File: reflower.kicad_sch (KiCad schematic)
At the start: 46 parts, among them J1 Jack-DC, SW1 RotaryEncoder_Switch, U1 AT32UC3B0256, U2 NCP1117-3.3, U3 MAX6675ISA+

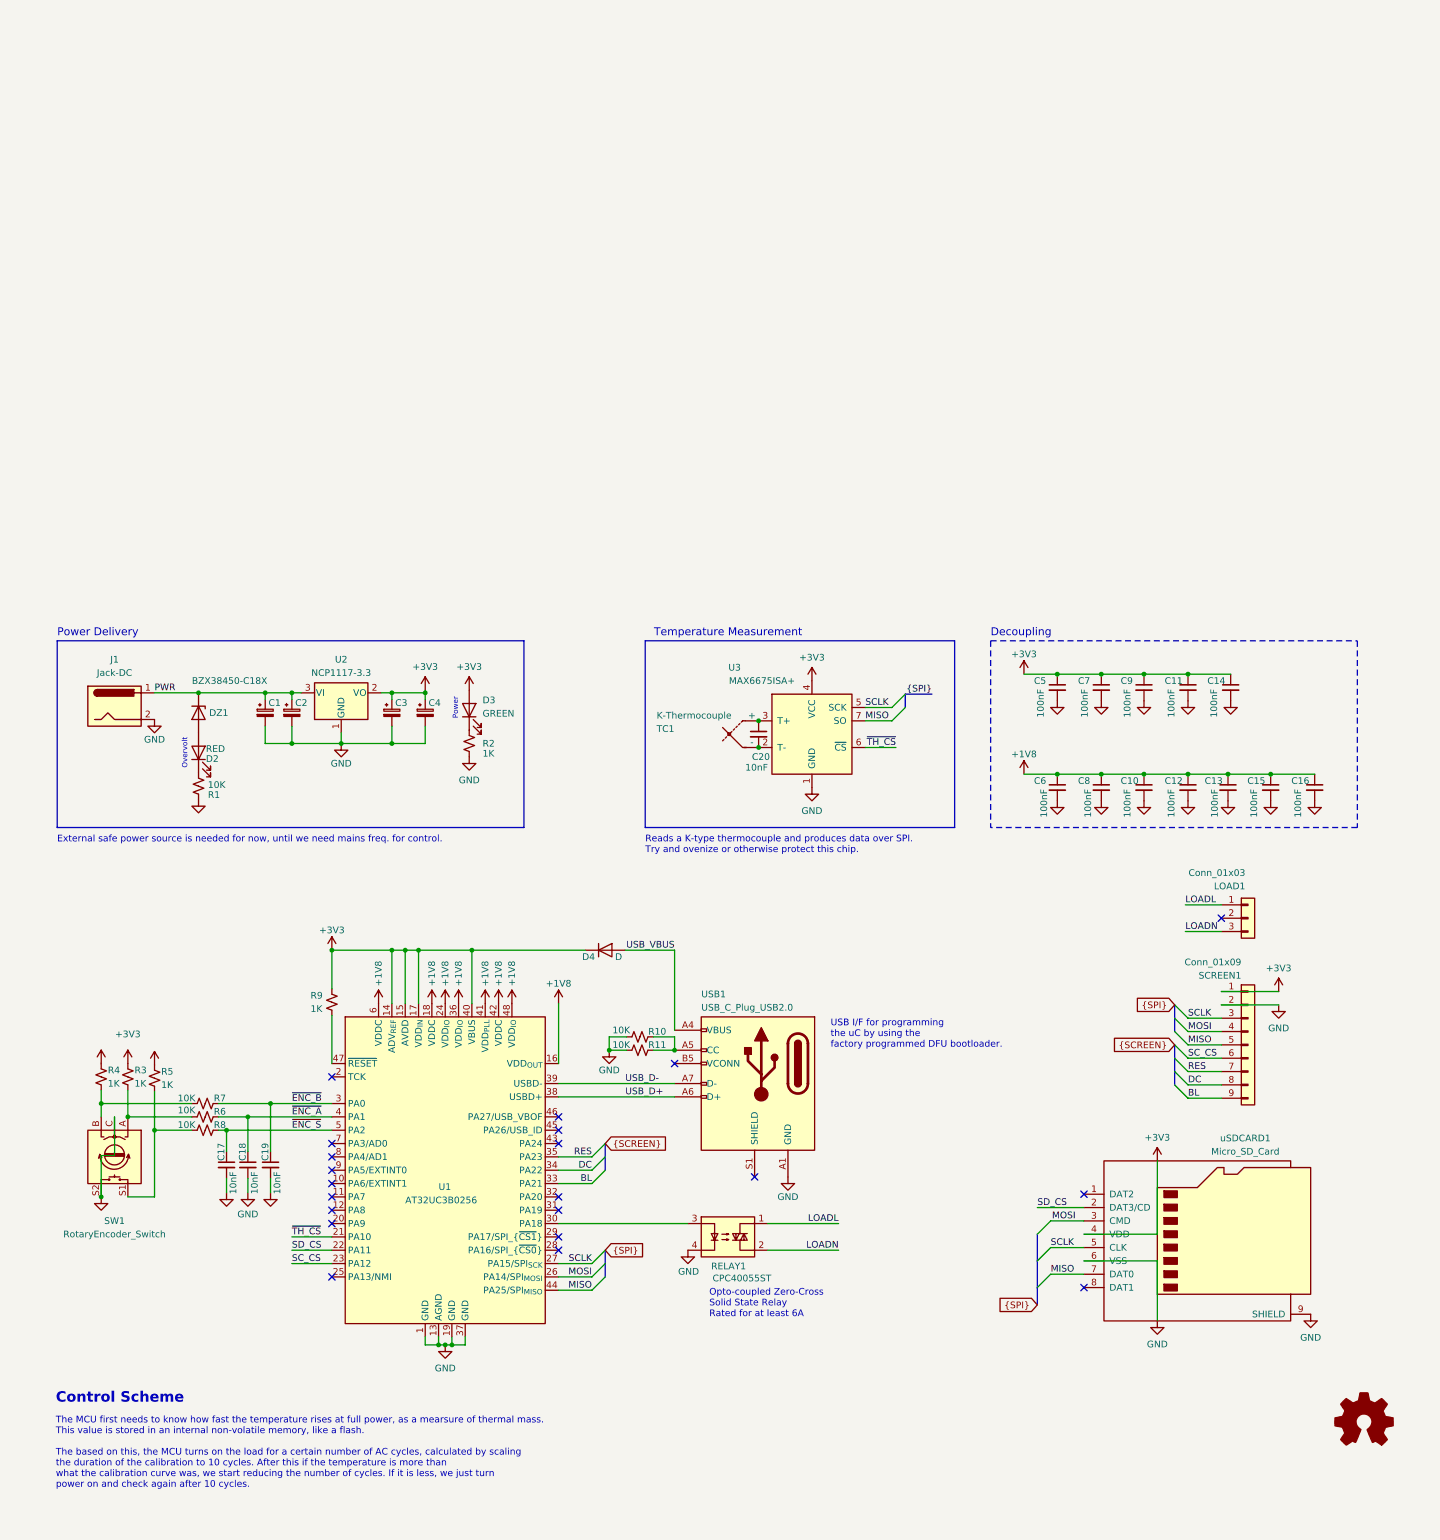
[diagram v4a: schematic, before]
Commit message: Revise to use STM32
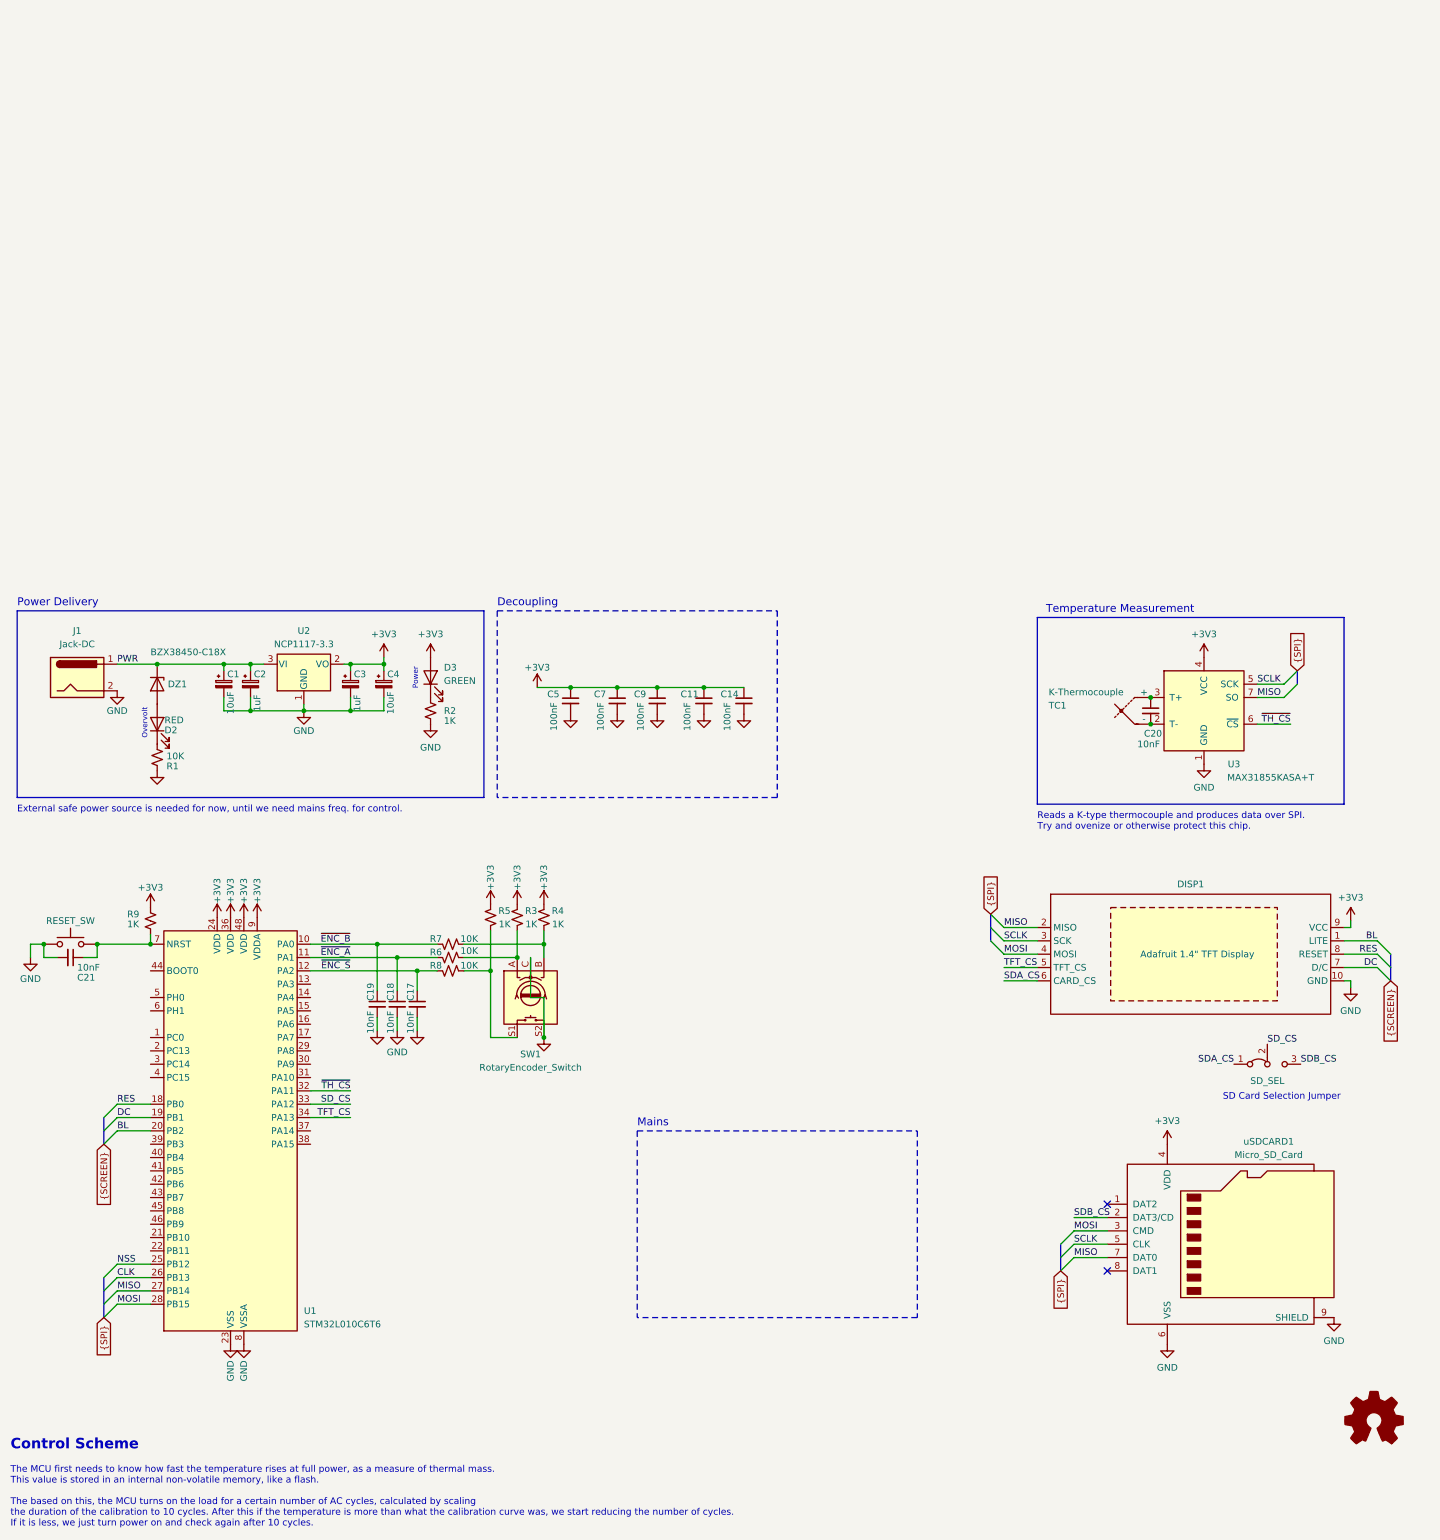
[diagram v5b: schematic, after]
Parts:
- removed C10, C12, C13, C15, C16, C6, C8: 100nF, Capacitor_SMD:C_0603_1608Metric, symbol Device:C_Small
- removed D4: D, Diode_SMD:D_0603_1608Metric, symbol Device:D
- removed LOAD1: Conn_01x03, TerminalBlock_Phoenix:TerminalBlock_Phoenix_MKDS-1,5-3_1x03_P5.00mm_Horizontal, symbol Connector_Generic:Conn_01x03
- removed R10, R11: 10K, Resistor_SMD:R_0603_1608Metric, symbol Device:R_Small_US
- removed RELAY1: CPC40055ST, SolidStateRelay:IXYS CPC40055ST, symbol Relay_SolidState:34.81-8240
- removed SCREEN1: Conn_01x09, Connector_PinHeader_2.54mm:PinHeader_1x09_P2.54mm_Horizontal, symbol Connector_Generic:Conn_01x09
- removed U1: AT32UC3B0256, Package_QFP:TQFP-48_7x7mm_P0.5mm, symbol AVR32:AT32UC3B0256
- removed USB1: USB_C_Plug_USB2.0, Connector_USB:USB_C_Receptacle_Amphenol_12401548E4-2A, symbol Connector:USB_C_Plug_USB2.0
- added C21: 10nF, Capacitor_SMD:C_0603_1608Metric, symbol Device:C_Small
- added DISP1: Adafruit 1.4" TFT Display, Connector_PinHeader_2.54mm:PinHeader_1x10_P2.54mm_Vertical, symbol Display_Graphic:Adafruit_358_TFT
- added RESET_SW: SW_Push, symbol Switch:SW_Push
- added SD_SEL: Jumper_3_Bridged12, Connector_PinHeader_2.54mm:PinHeader_1x03_P2.54mm_Vertical, symbol Jumper:Jumper_3_Bridged12
- added U1: STM32L010C6T6, Package_QFP:LQFP-48_7x7mm_P0.5mm, symbol MCU_ST_STM32L0:STM32L010C6Tx
- C1, C4: value (none) -> 10uF; footprint (none) -> Capacitor_THT:CP_Radial_D5.0mm_P2.00mm
- C2, C3: value (none) -> 1uF; footprint (none) -> Capacitor_THT:CP_Radial_D5.0mm_P2.00mm
- U3: value MAX6675ISA+ -> MAX31855KASA+T
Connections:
- net +3V3: now also DISP1.9 (VCC), U1.24 (VDD), U1.36 (VDD), U1.48 (VDD), U1.9 (VDDA)
- net BL: now also DISP1.1 (LITE), U1.20 (PB2)
- net DC: now also DISP1.7 (D/C), U1.19 (PB1)
- net GND: now also C21.2, DISP1.10 (GND), RESET_SW.1, U1.23 (VSS), U1.35 (VSS), U1.47 (VSS), U1.8 (VSSA)
- net MISO: now also DISP1.2 (MISO), U1.27 (PB14)
- net MOSI: now also DISP1.4 (MOSI), U1.28 (PB15)
- net RES: now also DISP1.8 (RESET), U1.18 (PB0)
- net SCLK: now also DISP1.3 (SCK)
- net SD_CS: now also SD_SEL.2 (C), U1.33 (PA12); no longer uSDCARD1.2 (DAT3/CD)
- net ~{ENC_A}: now also U1.11 (PA1)
- net ~{ENC_B}: now also U1.10 (PA0)
- net ~{ENC_S}: now also U1.12 (PA2)
- net ~{TH_CS}: now also U1.32 (PA11)
- net at R9.2: now also C21.1, RESET_SW.2, U1.7 (NRST)
- new net CLK: U1.26 (PB13)
- new net NSS: U1.25 (PB12)
- new net SDA_CS: DISP1.6 (CARD_CS), SD_SEL.1 (A)
- new net SDB_CS: SD_SEL.3 (B), uSDCARD1.2 (DAT3/CD)
- new net TFT_CS: DISP1.5 (TFT_CS), U1.34 (PA13)
- no-connect marks 21 -> 2
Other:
- note added: "Mains"
- note added: "SD Card Selection Jumper"
- note added: "The MCU first needs to know how fast the temperature rises at full power, as a measure of thermal mass. This value is stored in an internal non-volatile memory, like a flash. The based on this, the MCU turns on the load for a certain number of AC cycles, calculated by scaling the duration of the calibration to 10 cycles. After this if the temperature is more than what the calibration curve was, w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"
- note removed: "Opto-coupled Zero-Cross Solid State Relay Rated for at least 6A"
- note removed: "The MCU first needs to know how fast the temperature rises at full power, as a mearsure of thermal mass. This value is stored in an internal non-volatile memory, like a flash. The based on this, the MCU turns on the load for a certain number of AC cycles, calculated by scaling the duration of the calibration to 10 cycles. After this if the temperature is more than what the calibration curve was, 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"
- note removed: "USB I/F for programming the uC by using the factory programmed DFU bootloader."
- moved on the sheet: C1, C11, C14, C17, C18, C19, C2, C20, C3, C4, C5, C7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

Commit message: Redo Power supply
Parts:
- removed J1: Jack-DC, TerminalBlock_Phoenix:TerminalBlock_Phoenix_MKDS-1,5-2_1x02_P5.00mm_Horizontal, symbol Connector:Jack-DC
- removed U2: NCP1117-3.3, Package_TO_SOT_SMD:SOT-223-3_TabPin2, symbol Regulator_Linear:NCP1117-3.3_SOT223
- added C15: 10uF, Capacitor_THT:CP_Radial_D5.0mm_P2.00mm, symbol Device:C_Polarized_Small
- added D3: B380C2300-1500B, Diode_SMD:Diode_Bridge_Diotec_ABS, symbol Diode_Bridge:B380C2300-1500B
- added D4: 1N4007, Diode_THT:D_DO-41_SOD81_P10.16mm_Horizontal, symbol Diode:1N4007
- added DZ3: BZX38450-C6V2, Diode_SMD:D_SOD-323, symbol Device:D_Zener
- added PROG1: Conn_01x06, Connector_PinHeader_2.54mm:PinHeader_1x06_P2.54mm_Vertical, symbol Connector_Generic:Conn_01x06
- added PROG2: PROG, symbol Connector_Generic_Shielded:Conn_01x06_Shielded
- added Q1: IRG4PF50W, Package_TO_SOT_THT:TO-247-3_Vertical, symbol Transistor_IGBT:IRG4PF50W
- added R10, R12: 10K, symbol Device:R_Small_US
- added R11: 1K, symbol Device:R_Small_US
- added U1: NCP1117-3.3, Package_TO_SOT_SMD:SOT-223-3_TabPin2, symbol Regulator_Linear:NCP1117-3.3_SOT223
- added U4: 4N25, Package_DIP:DIP-6_W7.62mm, symbol Isolator:4N25
- added U5: ZXGD3006E6, Package_TO_SOT_SMD:SOT-23-6_Handsoldering, symbol Driver_FET:ZXGD3006E6
- C3: value 1uF -> 10uF
- C4: value 10uF -> 1uF
- ROT_SW1: renamed from SW1; value RotaryEncoder_Switch -> PEC11R-4215F-S0024
- renumbered C20 to C10, C21 to C11, C19 to C12, C18 to C13, C17 to C14, C7 to C6, C9 to C7, C11 to C8, C14 to C9, R5 to R3, R3 to R4, R4 to R5, R9 to R6, R6 to R8, R8 to R9, RESET_SW to RESET_SW1, SD_SEL to SD_SEL1, U3 to U2, U1 to U3
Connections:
- net +3V3: now also R10.2, U1.2 (VO), U5.1 (VCC)
- net CLK: now also PROG1.3 (Pin_3), PROG2.3 (Pin_3)
- net GND: now also C15.2, D3.1 (-), DZ3.2 (A), PROG1.6 (Pin_6), PROG2.6 (Pin_6), PROG2.SH (Shield), U1.1 (GND), U4.4, U5.3 (VEE)
- net MISO: now also PROG1.4 (Pin_4), PROG2.4 (Pin_4)
- net MOSI: now also PROG1.5 (Pin_5), PROG2.5 (Pin_5)
- net NSS: now also PROG1.2 (Pin_2), PROG2.2 (Pin_2)
- net ZERO: now reaches U3.37 (PA14)
- net ZERO: now also R10.1, U4.5
- net TRIG: now reaches U3.38 (PA15)
- net TRIG: now also U5.2 (IN)
- net PWR: no longer names the net of C1.1, C2.1
- net PWR: now also D3.3 (+); no longer DZ1.1 (K)
- new net: D4.2 (A), Q1.1 (G), R11.1, R12.1
- new net: D4.1 (K), R11.2, U5.4 (SINK), U5.6 (SRC)
- new net AC: D3.2, U4.1
- new net GNDPWR: D3.4, U4.2
- new net VDC: C15.1, DZ3.1 (K), PROG1.1 (Pin_1), PROG2.1 (Pin_1), U1.3 (VI)
- no-connect marks 2 -> 3
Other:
- note added: "5V Zener Regulator"
- note added: "Handles power delivery to this board via multiple sources. Either via the mains supply, the SPI header, or an external source."
- note added: "Logic Supply"
- note added: "Mains 220VAC"
- note added: "Overvolatge"
- note added: "Power LED"
- note added: "SD Card Selection"
- note added: "Zero-Crossing Detection"
- note removed: "Mains"
- note removed: "Overvolt"
- note removed: "Power"
- note removed: "SD Card Selection Jumper"
- moved on the sheet: C10, C11, C12, C13, C14, C5, C6, C7, C8, C9, DISP1, R3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

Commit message: Power
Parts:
- added J1: Screw_Terminal_01x02, symbol Connector:Screw_Terminal_01x02
- renumbered D2 to LED1, D3 to LED2
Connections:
- net AC: no longer D3.2
- net GNDPWR: now also J1.2 (Pin_2)
- net at C1.1, C2.1, D3.3 (+): now also DZ1.1 (K)
- new net VSS: D3.2, J1.1 (Pin_1)
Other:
- note added: "18V Zener Regulator"
- moved on the sheet: C1, C15, C2, C3, C4, D3, DZ1, DZ3, LED1, R1, U1

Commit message: External power
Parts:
- removed DZ3: BZX38450-C6V2, Diode_SMD:D_SOD-323, symbol Device:D_Zener
- added J2: Screw_Terminal_01x02, symbol Connector:Screw_Terminal_01x02
- added J3: Barrel_Jack, symbol Connector:Barrel_Jack
- DZ1: value BZX38450-C18X -> BZX38450-C5V1
- renumbered C9 to C1, C6 to C10, C5 to C11, C11 to C12, C12 to C13, C13 to C14, C14 to C15, C8 to C2, C10 to C3, C7 to C4, C1 to C5, C2 to C6, C3 to C7, C4 to C8, C15 to C9, D3 to D1, D4 to D3, LED2 to LED1, LED1 to LED2, R2 to R1, R1 to R2, U2 to U1, U1 to U2, U5 to U4, U4 to U5
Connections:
- net AC: now also D1.2, J1.1 (Pin_1); no longer U5.1
- net GND: now also J2.2 (Pin_2), J3.2
- net VDC: now also C5.1, C6.1, DZ1.1 (K), J2.1 (Pin_1), J3.1
- net VSS: now also D1.3 (+), U5.1; no longer D1.2, J1.1 (Pin_1)
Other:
- note added: "External safe DC power source is needed for now, until can use mains for logic supply."
- note removed: "18V Zener Regulator"
- note removed: "External safe power source is needed for now, until we need mains freq. for control."
- moved on the sheet: C3, C5, C6, C7, C8, C9, DZ1, LED2, R2, SD_SEL1, TC1, U1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
